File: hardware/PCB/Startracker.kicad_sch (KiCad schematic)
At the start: 0 parts

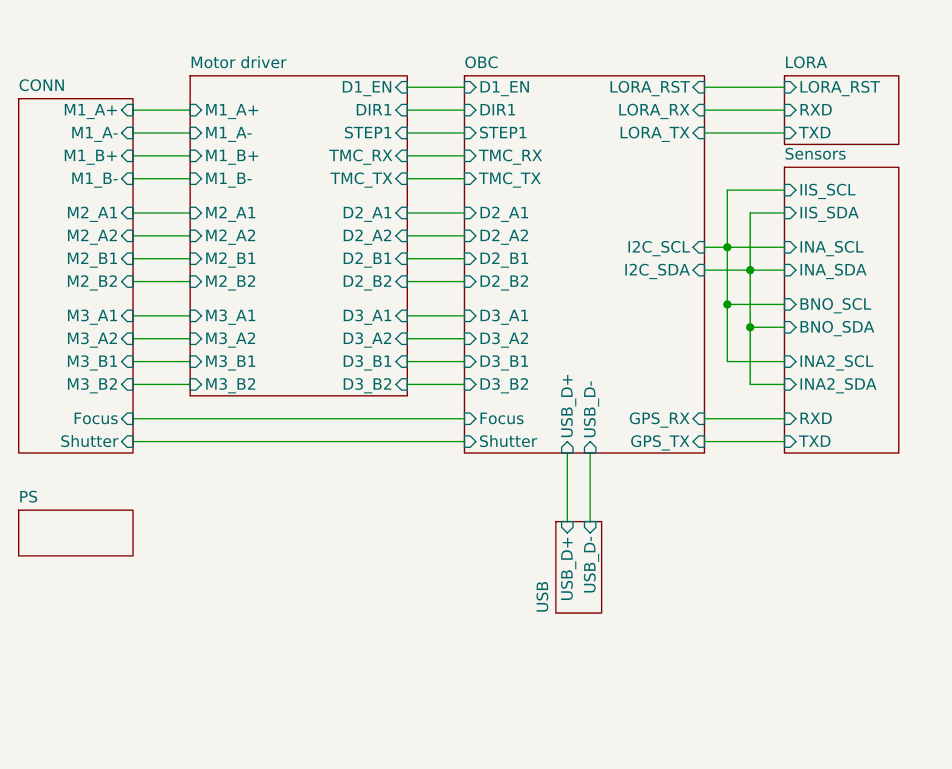
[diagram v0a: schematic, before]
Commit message: Added connection for external IMU to PCB
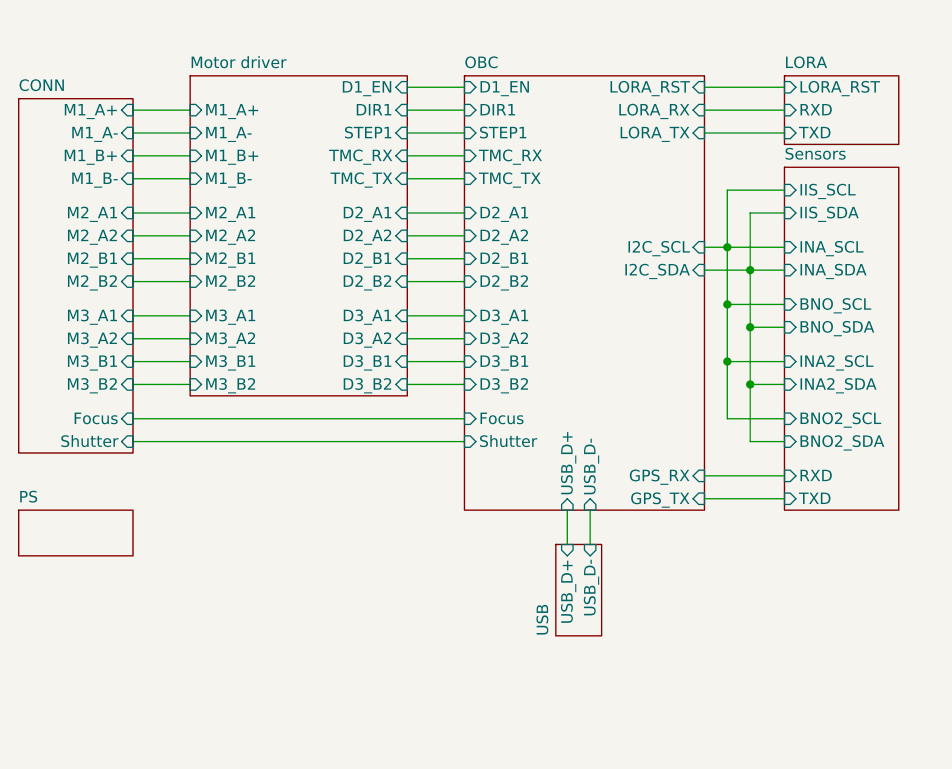
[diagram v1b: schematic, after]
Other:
- sheet Sensors ports: added BNO2_SCL, BNO2_SDA; removed none
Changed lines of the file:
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@@
+	)
+	(junction
+		(at 127 59.69)
+		(diameter 0)
+		(color 0 0 0 0)
 	)
 	(junction
@@
 	)
 	(junction
+		(at 124.46 57.15)
+		(diameter 0)
+		(color 0 0 0 0)
+	)
+	(junction
 		(at 127 46.99)
 		(diameter 0)
@@
 	(wire
 		(pts
+			(xy 124.46 63.5) (xy 124.46 57.15)
+		)
+		(stroke
+			(width 0)
+			(type default)
+		)
+	)
+	(wire
+		(pts
 			(xy 88.9 59.69) (xy 95.25 59.69)
 		)
@@
 	(wire
 		(pts
+			(xy 109.22 73.66) (xy 109.22 77.47)
+		)
+		(stroke
+			(width 0)
+			(type default)
+		)
+	)
+	(wire
+		(pts
+			(xy 127 66.04) (xy 127 59.69)
+		)
+		(stroke
+			(width 0)
+			(type default)
+		)
+	)
+	(wire
+		(pts
 			(xy 121.92 29.21) (xy 130.81 29.21)
 		)
@@
 	(wire
 		(pts
-			(xy 109.22 67.31) (xy 109.22 74.93)
-		)
-		(stroke
-			(width 0)
-			(type default)
-		)
-	)
-	(wire
-		(pts
 			(xy 124.46 38.1) (xy 124.46 44.45)
 		)
@@
 	(wire
 		(pts
-			(xy 106.68 67.31) (xy 106.68 74.93)
-		)
-		(stroke
-			(width 0)
-			(type default)
-		)
-	)
-	(wire
-		(pts
 			(xy 58.42 54.61) (xy 64.77 54.61)
 		)
@@
 	(wire
 		(pts
+			(xy 130.81 66.04) (xy 127 66.04)
+		)
+		(stroke
+			(width 0)
+			(type default)
+		)
+	)
+	(wire
+		(pts
 			(xy 124.46 44.45) (xy 130.81 44.45)
 		)
@@
 	(wire
 		(pts
-			(xy 121.92 63.5) (xy 130.81 63.5)
+			(xy 121.92 69.85) (xy 130.81 69.85)
 		)
 		(stroke
@@
 	(wire
 		(pts
-			(xy 121.92 66.04) (xy 130.81 66.04)
+			(xy 121.92 72.39) (xy 130.81 72.39)
 		)
 		(stroke
@@
 	(wire
 		(pts
+			(xy 130.81 63.5) (xy 124.46 63.5)
+		)
+		(stroke
+			(width 0)
+			(type default)
+		)
+	)
+	(wire
+		(pts
 			(xy 88.9 45.72) (xy 95.25 45.72)
+		)
+		(stroke
+			(width 0)
+			(type default)
+		)
+	)
+	(wire
+		(pts
+			(xy 106.68 73.66) (xy 106.68 77.47)
 		)
 		(stroke
@@
 	)
 	(sheet
-		(at 105.41 74.93)
+		(at 105.41 77.47)
 		(size 5.08 10.16)
 		(exclude_from_sim no)
@@
 		)
 		(property "Sheetname" "USB"
-			(at 104.6984 85.09 90)
+			(at 104.6984 87.63 90)
 			(effects
 				(font
@@
 		)
 		(property "Sheetfile" "usb.kicad_sch"
-			(at 111.0746 85.09 90)
+			(at 111.0746 87.63 90)
 			(effects
 				(font
@@
 		)
 		(pin "USB_D+" input
-			(at 106.68 74.93 90)
+			(at 106.68 77.47 90)
 			(effects
 				(font
@@
 		)
 		(pin "USB_D-" input
-			(at 109.22 74.93 90)
+			(at 109.22 77.47 90)
 			(effects
 				(font
@@
 	(sheet
 		(at 95.25 25.4)
-		(size 26.67 41.91)
+		(size 26.67 48.26)
 		(exclude_from_sim no)
 		(in_bom yes)
@@
 		)
 		(property "Sheetfile" "obc.kicad_sch"
-			(at 95.25 67.8946 0)
+			(at 95.25 74.2446 0)
 			(effects
 				(font
@@
 		)
 		(pin "GPS_RX" input
-			(at 121.92 63.5 0)
+			(at 121.92 69.85 0)
 			(effects
 				(font
@@
 		)
 		(pin "GPS_TX" input
-			(at 121.92 66.04 0)
+			(at 121.92 72.39 0)
 			(effects
 				(font
@@
 		)
 		(pin "USB_D+" input
-			(at 106.68 67.31 270)
+			(at 106.68 73.66 270)
 			(effects
 				(font
@@
 		)
 		(pin "USB_D-" input
-			(at 109.22 67.31 270)
+			(at 109.22 73.66 270)
 			(effects
 				(font
@@
 	(sheet
 		(at 130.81 35.56)
-		(size 12.7 31.75)
+		(size 12.7 38.1)
 		(exclude_from_sim no)
 		(in_bom yes)
@@
 		)
 		(property "Sheetfile" "sensors.kicad_sch"
-			(at 130.81 67.8946 0)
+			(at 130.81 74.2446 0)
 			(effects
 				(font
@@
 		)
 		(pin "RXD" input
-			(at 130.81 63.5 180)
+			(at 130.81 69.85 180)
 			(effects
 				(font
@@
 		)
 		(pin "TXD" input
-			(at 130.81 66.04 180)
+			(at 130.81 72.39 180)
 			(effects
 				(font
@@
 			(effects
 				(font
+					(size 1.27 1.27)
+				)
+				(justify left)
+			)
+		)
+		(pin "BNO2_SCL" input
+			(at 130.81 63.5 180)
+			(effects
+				(font
+					(size 1.27 1.27)
+				)
+				(justify left)
+			)
+		)
+		(pin "BNO2_SDA" input
+			(at 130.81 66.04 180)
+			(effects
+				(font

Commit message: Added I2C expander for motor drivers and changed LoRa module
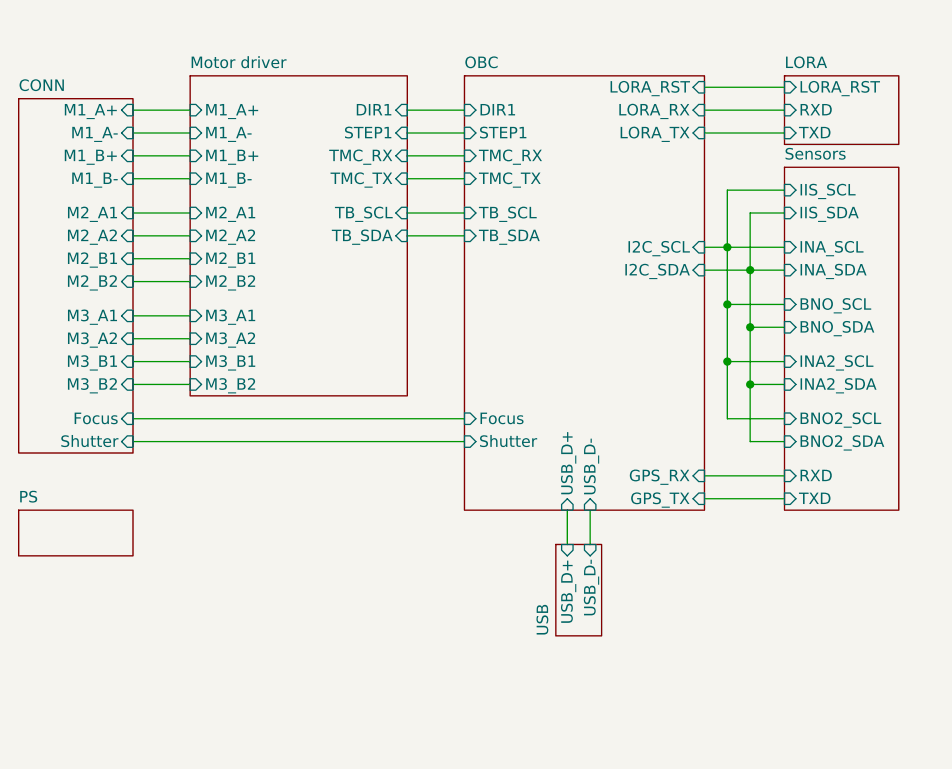
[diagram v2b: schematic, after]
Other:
- sheet Motor driver ports: added TB_SCL, TB_SDA; removed D1_EN, D2_A1, D2_A2, D2_B1, D2_B2, D3_A1, D3_A2, D3_B1, D3_B2
- sheet OBC ports: added TB_SCL, TB_SDA; removed D1_EN, D2_A1, D2_A2, D2_B1, D2_B2, D3_A1, D3_A2, D3_B1, D3_B2

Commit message: Finished schematic for LoRa, added BME280
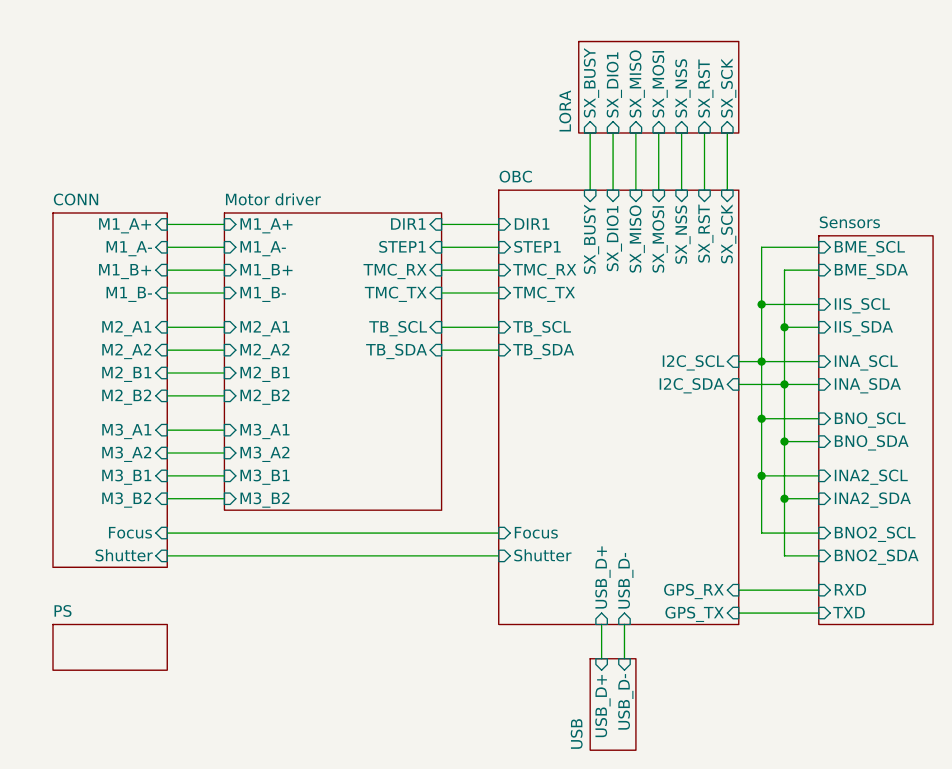
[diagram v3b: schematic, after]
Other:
- sheet LORA ports: added SX_BUSY, SX_DIO1, SX_MISO, SX_MOSI, SX_NSS, SX_RST, SX_SCK; removed LORA_RST, RXD, TXD
- sheet OBC ports: added SX_BUSY, SX_DIO1, SX_MISO, SX_MOSI, SX_NSS, SX_RST, SX_SCK; removed LORA_RST, LORA_RX, LORA_TX
- sheet Sensors ports: added BME_SCL, BME_SDA; removed none

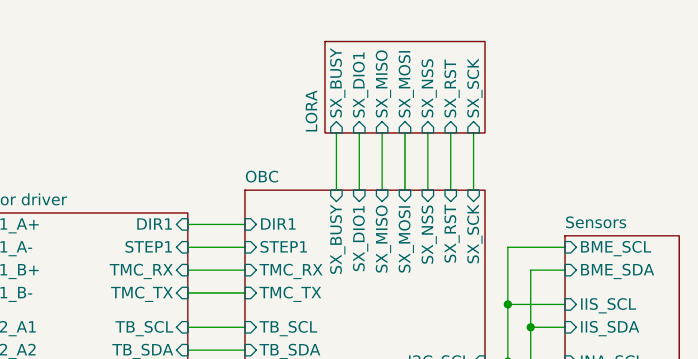
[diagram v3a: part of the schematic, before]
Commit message: Rerouted changes on the PCB layout, Routed LoRa
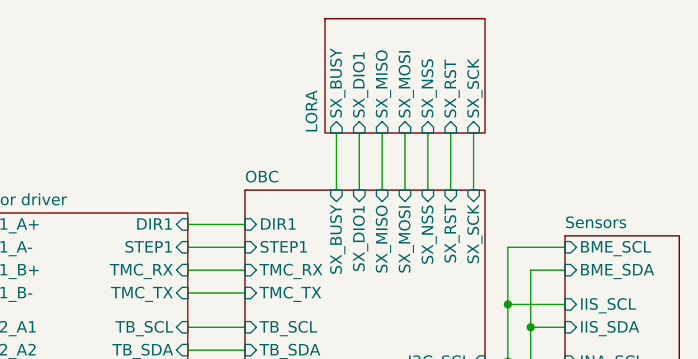
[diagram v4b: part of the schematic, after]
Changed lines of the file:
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@@
 	)
 	(sheet
-		(at 107.95 21.59)
-		(size 17.78 10.16)
+		(at 107.95 19.05)
+		(size 17.78 12.7)
 		(exclude_from_sim no)
 		(in_bom yes)

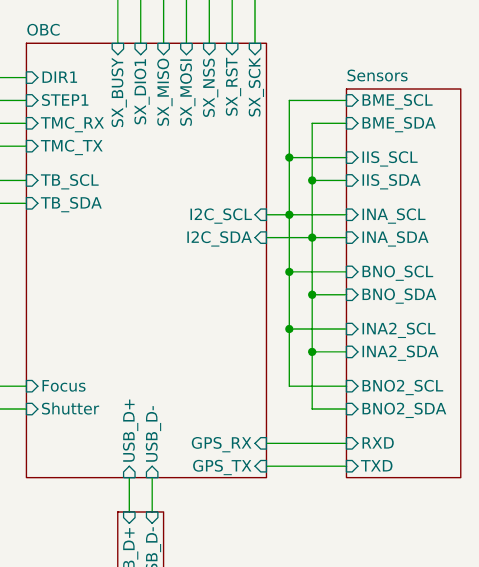
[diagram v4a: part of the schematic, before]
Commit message: Routed VL53L4CD
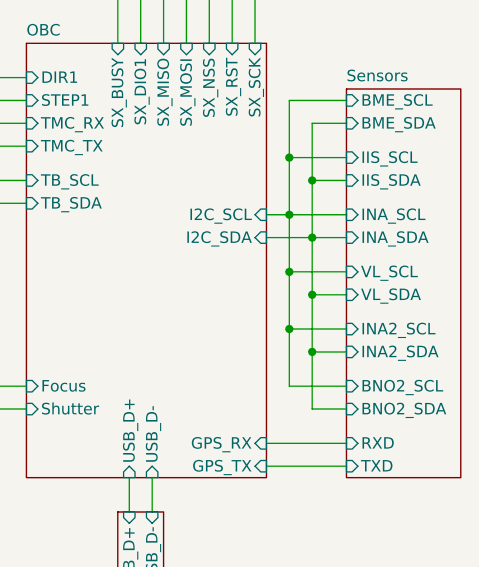
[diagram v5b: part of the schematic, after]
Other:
- sheet Sensors ports: added VL_SCL, VL_SDA; removed BNO_SCL, BNO_SDA
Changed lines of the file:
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@@
-			)
-		)
-		(pin "BNO_SCL" input
-			(at 134.62 63.5 180)
-			(effects
-				(font
-					(size 1.27 1.27)
-				)
-				(justify left)
-			)
-		)
-		(pin "BNO_SDA" input
-			(at 134.62 66.04 180)
-			(effects
-				(font
-					(size 1.27 1.27)
-				)
-				(justify left)
 			)
 		)
@@
 			(effects
 				(font
+					(size 1.27 1.27)
+				)
+				(justify left)
+			)
+		)
+		(pin "VL_SCL" input
+			(at 134.62 63.5 180)
+			(effects
+				(font
+					(size 1.27 1.27)
+				)
+				(justify left)
+			)
+		)
+		(pin "VL_SDA" input
+			(at 134.62 66.04 180)
+			(effects
+				(font

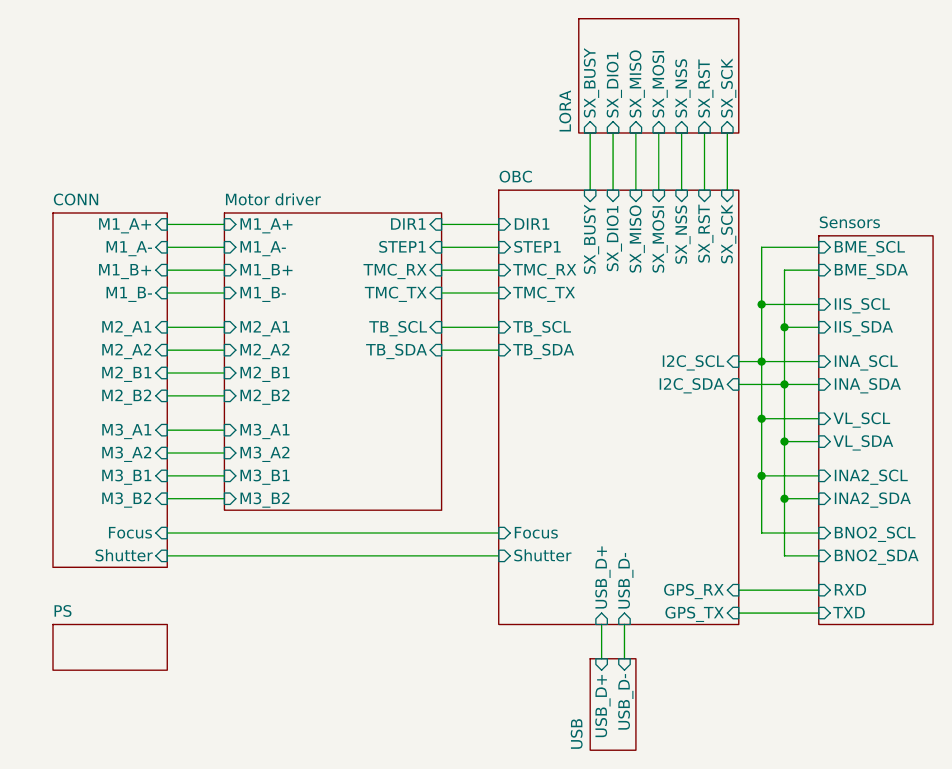
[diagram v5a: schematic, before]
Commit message: added external ToF instead of on-PCB
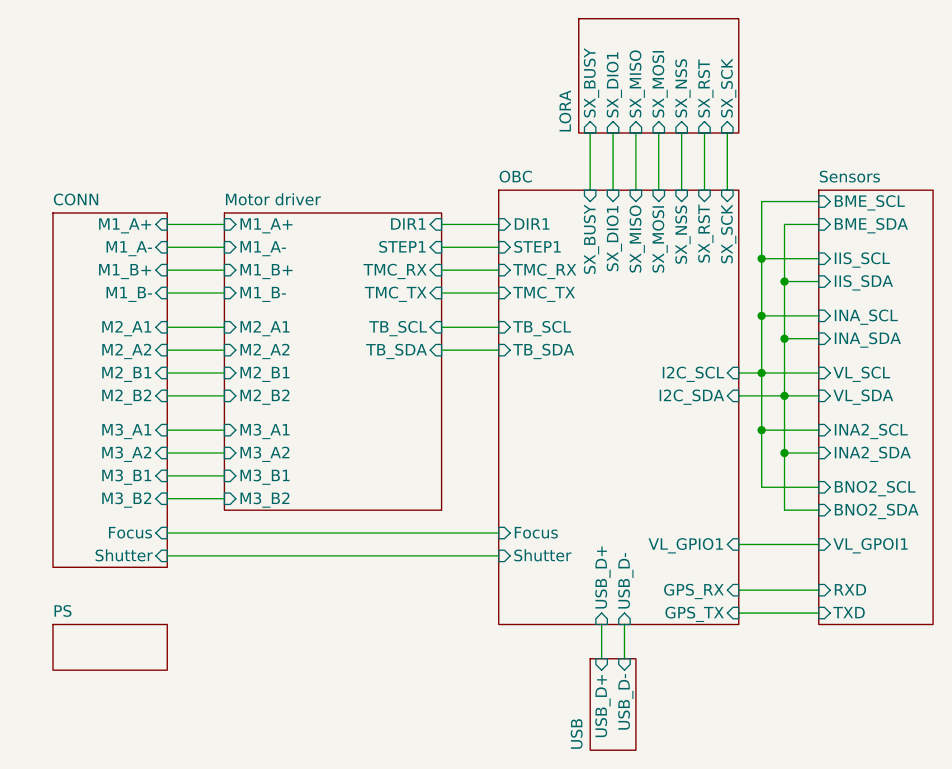
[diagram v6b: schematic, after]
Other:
- sheet OBC ports: added VL_GPIO1; removed none
- sheet Sensors ports: added VL_GPOI1; removed none
